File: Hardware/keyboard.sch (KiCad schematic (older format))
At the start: 57 parts, among them M1 Tab, M10 O, M11 P, M12 Backspace, M13 Esc, M14 A, M15 S, M16 D, M17 F, M18 G, M19 H, M2 Q, M20 J, M21 K, M22 L, M23 ;, M24 ', M25 Shift, M26 Z, M27 X, M28 C, M29 V, M3 W, M30 B, M31 N, M32 M, M33 ,, M34 ., M35 /, M36 Enter, M37 Blnk, M38 Ctrl, M39 Alt, M4 E, M40 Super, M41 Down, M42 Space, M43 Up, M44 L_Ar, M45 D_Ar, M46 U_Ar, M47 R_Ar, M5 R, M6 T, M7 Y, M8 U, M9 I, U1 ROW_1, U2 ROW_2, U3 ROW_3

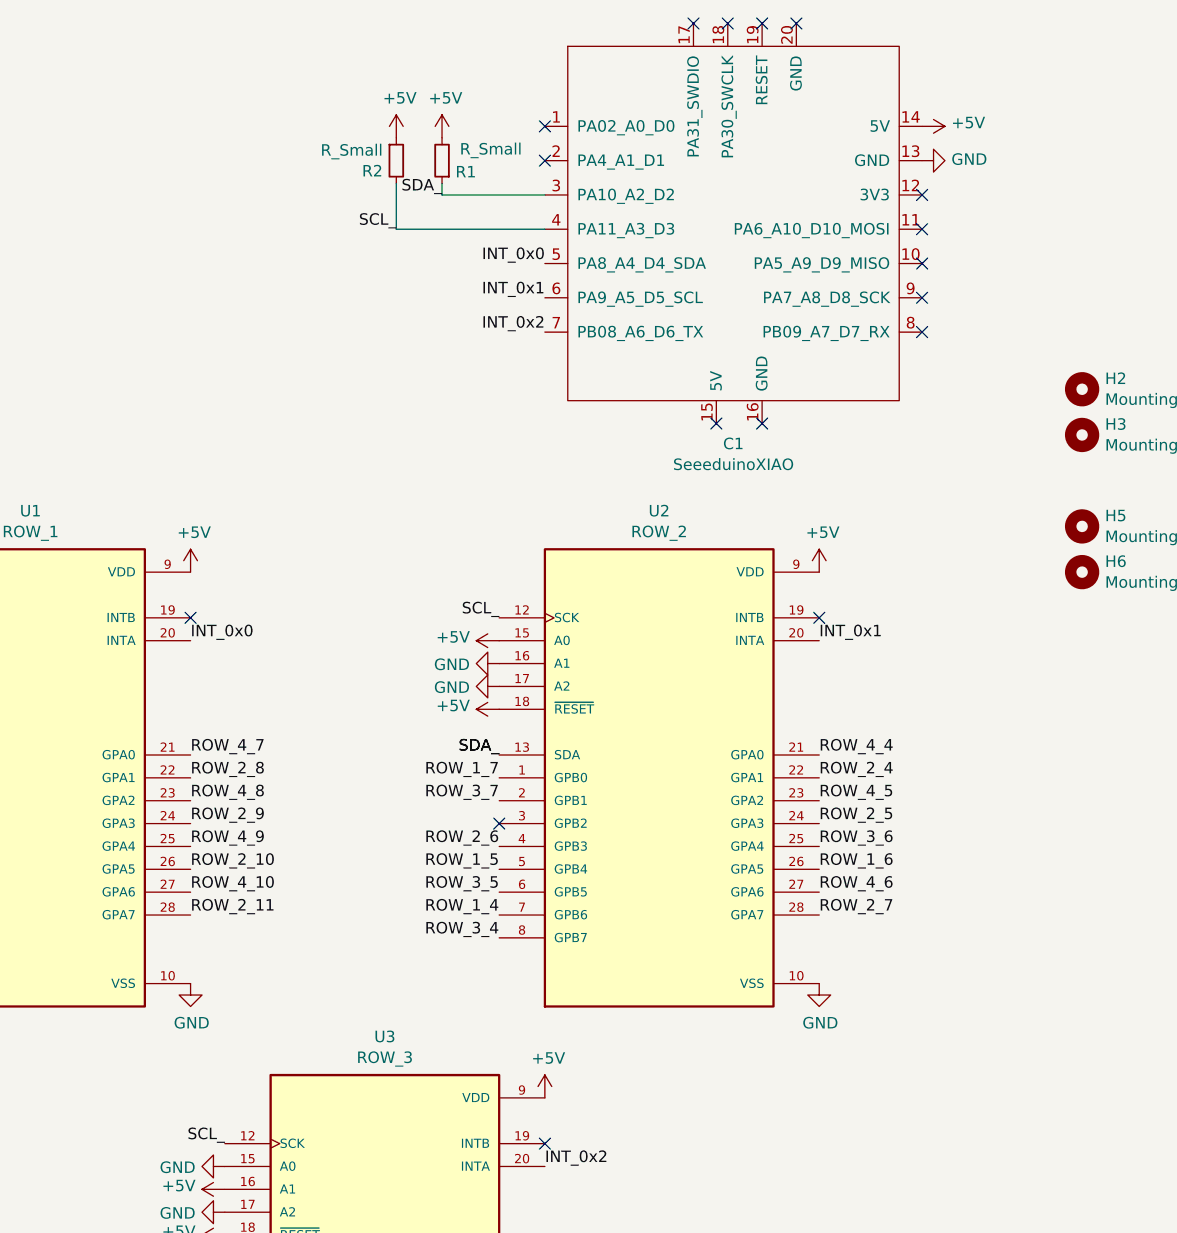
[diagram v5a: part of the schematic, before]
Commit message: Swapped SDA and SCL pins.
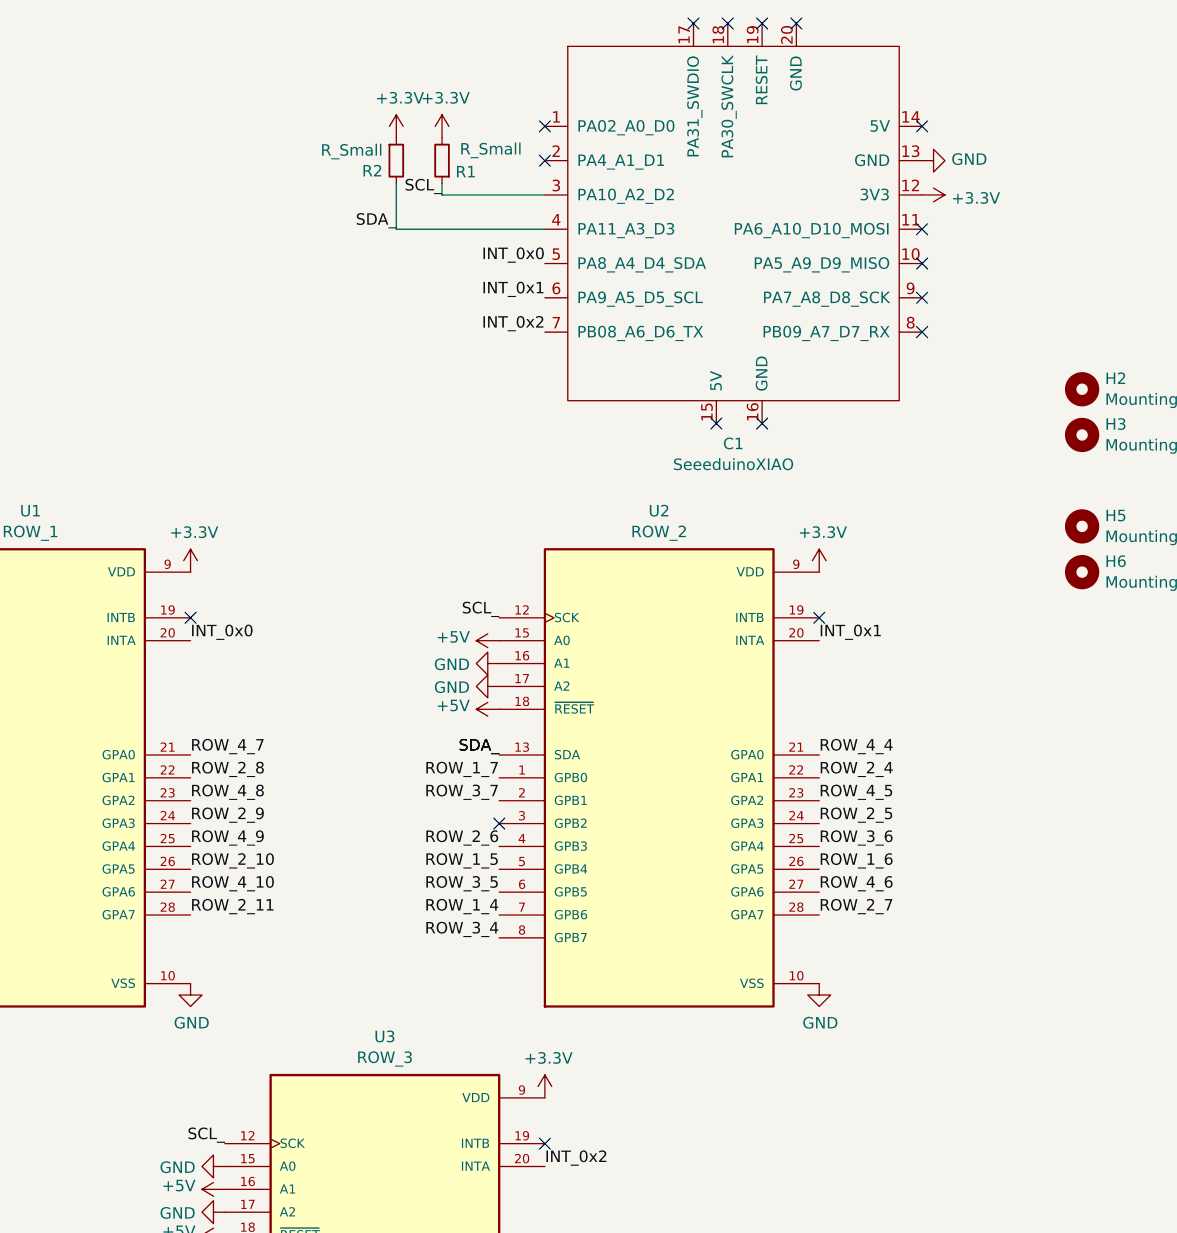
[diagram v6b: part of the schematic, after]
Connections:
- net +5V: no longer C1.14 (5V), R1.2, R2.1, U1.9 (VDD), U2.9 (VDD), U3.9 (VDD)
- net SCL_: now also C1.3 (PA10_A2_D2), R1.1; no longer C1.4 (PA11_A3_D3), R2.2
- net SDA_: now also C1.4 (PA11_A3_D3), R2.2; no longer C1.3 (PA10_A2_D2), R1.1
- net +3V3: now reaches C1.12 (3V3)
- net +3V3: now also R1.2, R2.1, U1.9 (VDD), U2.9 (VDD), U3.9 (VDD)
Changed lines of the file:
@@
 SDA_
-$Comp
-L power:+5V #PWR023
-U 1 1 617FE266
-P 3050 2950
-F 0 "#PWR023" H 3050 2800 50  0001 C CNN
-F 1 "+5V" H 3065 3123 50  0000 C CNN
-F 2 "" H 3050 2950 50  0001 C CNN
-F 3 "" H 3050 2950 50  0001 C CNN
-	1    3050 2950
-	1    0    0    -1
-$EndComp
-$Comp
-L power:+5V #PWR07
-U 1 1 617FF047
-P 4600 5250
-F 0 "#PWR07" H 4600 5100 50  0001 C CNN
-F 1 "+5V" H 4615 5423 50  0000 C CNN
-F 2 "" H 4600 5250 50  0001 C CNN
-F 3 "" H 4600 5250 50  0001 C CNN
-	1    4600 5250
-	1    0    0    -1
-$EndComp
-$Comp
-L power:+5V #PWR09
-U 1 1 61800192
-P 5800 2950
-F 0 "#PWR09" H 5800 2800 50  0001 C CNN
-F 1 "+5V" H 5815 3123 50  0000 C CNN
-F 2 "" H 5800 2950 50  0001 C CNN
-F 3 "" H 5800 2950 50  0001 C CNN
-	1    5800 2950
-	1    0    0    -1
-$EndComp
 $Comp
 L power:GND #PWR016
@@
 Text Label 4600 1600 2    50   ~ 0
 INT_0x0
+Text Label 3950 1450 2    50   ~ 0
+SDA_
 Text Label 4150 1300 2    50   ~ 0
-SDA_
-Text Label 3950 1450 2    50   ~ 0
 SCL_
 Wire Wire Line
@@
 	-1   0    0    1
 $EndComp
-$Comp
-L power:+5V #PWR011
-U 1 1 617E9B2D
-P 3950 1050
-F 0 "#PWR011" H 3950 900 50  0001 C CNN
-F 1 "+5V" H 3965 1223 50  0000 C CNN
-F 2 "" H 3950 1050 50  0001 C CNN
-F 3 "" H 3950 1050 50  0001 C CNN
-	1    3950 1050
-	1    0    0    -1
-$EndComp
-$Comp
-L power:+5V #PWR012
-U 1 1 617EA5A5
-P 4150 1050
-F 0 "#PWR012" H 4150 900 50  0001 C CNN
-F 1 "+5V" H 4165 1223 50  0000 C CNN
-F 2 "" H 4150 1050 50  0001 C CNN
-F 3 "" H 4150 1050 50  0001 C CNN
-	1    4150 1050
-	1    0    0    -1
-$EndComp
 Wire Wire Line
 	4600 1300 4150 1300
@@
 	1    6250 1150
 	0    -1   -1   0
-$EndComp
-$Comp
-L power:+5V #PWR019
-U 1 1 617E451E
-P 6250 1000
-F 0 "#PWR019" H 6250 850 50  0001 C CNN
-F 1 "+5V" V 6265 1128 50  0000 L CNN
-F 2 "" H 6250 1000 50  0001 C CNN
-F 3 "" H 6250 1000 50  0001 C CNN
-	1    6250 1000
-	0    1    -1   0
 $EndComp
 $Comp
@@
 NoConn ~ 5400 550
 NoConn ~ 5250 550
-NoConn ~ 6250 1300
 Text Label 8950 1250 0    50   ~ 0
 ROW_1_0
@@
 	1    9650 2250
 	0    -1   -1   0
-$EndComp
-$Comp
-L keyboard-rescue:MCP23017T-E_SO-MCP23017-keyboard-rescue U1
-U 1 1 61A36BFE
-P 2350 3850
-F 0 "U1" H 2350 5017 50  0000 C CNN
-F 1 "ROW_1" H 2350 4926 50  0000 C CNN
-F 2 "Package_DIP:DIP-28_W7.62mm" H 2350 3850 50  0001 L BNN
-F 3 "" H 2350 3850 50  0001 L BNN
-F 4 "IPC7351B" H 2350 3850 50  0001 L BNN "STANDARD"
-F 5 "Microchip" H 2350 3850 50  0001 L BNN "MANUFACTURER"
-F 6 "" H 2350 3850 50  0001 L BNN "PARTREV"
-	1    2350 3850
-	1    0    0    -1
 $EndComp
 NoConn ~ 3050 3150
@@
 NoConn ~ 4600 1150
 NoConn ~ 4400 4050
+$Comp
+L power:+3.3V #PWR?
+U 1 1 619D6D30
+P 6250 1300
+F 0 "#PWR?" H 6250 1150 50  0001 C CNN
+F 1 "+3.3V" V 6265 1428 50  0000 L CNN
+F 2 "" H 6250 1300 50  0001 C CNN
+F 3 "" H 6250 1300 50  0001 C CNN
+	1    6250 1300
+	0    1    1    0
+$EndComp
+NoConn ~ 6250 1000
+$Comp
+L power:+3.3V #PWR?
+U 1 1 619DB794
+P 3950 1050
+F 0 "#PWR?" H 3950 900 50  0001 C CNN
+F 1 "+3.3V" H 3965 1223 50  0000 C CNN
+F 2 "" H 3950 1050 50  0001 C CNN
+F 3 "" H 3950 1050 50  0001 C CNN
+	1    3950 1050
+	1    0    0    -1
+$EndComp
+$Comp
+L power:+3.3V #PWR?
+U 1 1 619DD6B1
+P 4150 1050
+F 0 "#PWR?" H 4150 900 50  0001 C CNN
+F 1 "+3.3V" H 4165 1223 50  0000 C CNN
+F 2 "" H 4150 1050 50  0001 C CNN
+F 3 "" H 4150 1050 50  0001 C CNN
+	1    4150 1050
+	1    0    0    -1
+$EndComp
+$Comp
+L power:+3.3V #PWR?
+U 1 1 619DDAAC
+P 3050 2950
+F 0 "#PWR?" H 3050 2800 50  0001 C CNN
+F 1 "+3.3V" H 3065 3123 50  0000 C CNN
+F 2 "" H 3050 2950 50  0001 C CNN
+F 3 "" H 3050 2950 50  0001 C CNN
+	1    3050 2950
+	1    0    0    -1
+$EndComp
+$Comp
+L keyboard-rescue:MCP23017T-E_SO-MCP23017-keyboard-rescue U1
+U 1 1 61A36BFE
+P 2350 3850
+F 0 "U1" H 2350 5017 50  0000 C CNN
+F 1 "ROW_1" H 2350 4926 50  0000 C CNN
+F 2 "Package_DIP:DIP-28_W7.62mm" H 2350 3850 50  0001 L BNN
+F 3 "" H 2350 3850 50  0001 L BNN
+F 4 "IPC7351B" H 2350 3850 50  0001 L BNN "STANDARD"
+F 5 "Microchip" H 2350 3850 50  0001 L BNN "MANUFACTURER"
+F 6 "" H 2350 3850 50  0001 L BNN "PARTREV"
+	1    2350 3850
+	1    0    0    -1
+$EndComp
+$Comp
+L power:+3.3V #PWR?
+U 1 1 619DF3E7
+P 5800 2950
+F 0 "#PWR?" H 5800 2800 50  0001 C CNN
+F 1 "+3.3V" H 5815 3123 50  0000 C CNN
+F 2 "" H 5800 2950 50  0001 C CNN
+F 3 "" H 5800 2950 50  0001 C CNN
+	1    5800 2950
+	1    0    0    -1
+$EndComp
+$Comp
+L power:+3.3V #PWR?
+U 1 1 619DFBFC
+P 4600 5250
+F 0 "#PWR?" H 4600 5100 50  0001 C CNN
+F 1 "+3.3V" H 4615 5423 50  0000 C CNN
+F 2 "" H 4600 5250 50  0001 C CNN
+F 3 "" H 4600 5250 50  0001 C CNN
+	1    4600 5250
+	1    0    0    -1
+$EndComp
 $EndSCHEMATC
